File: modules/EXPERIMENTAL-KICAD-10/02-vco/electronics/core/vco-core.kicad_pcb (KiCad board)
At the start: 2 copper layers, 58 x 110 mm, 146 parts, among them J1 Conn_01x04, J2 Conn_02x05_Odd_Even, J3 Conn_02x05_Odd_Even, J4 Conn_01x02, J5 Conn_02x03_Odd_Even, J6 Conn_02x02_Counter_Clockwise, J8 Conn_01x07, Q1 BC847BS, Q2 MMBT3906, Q3 J111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

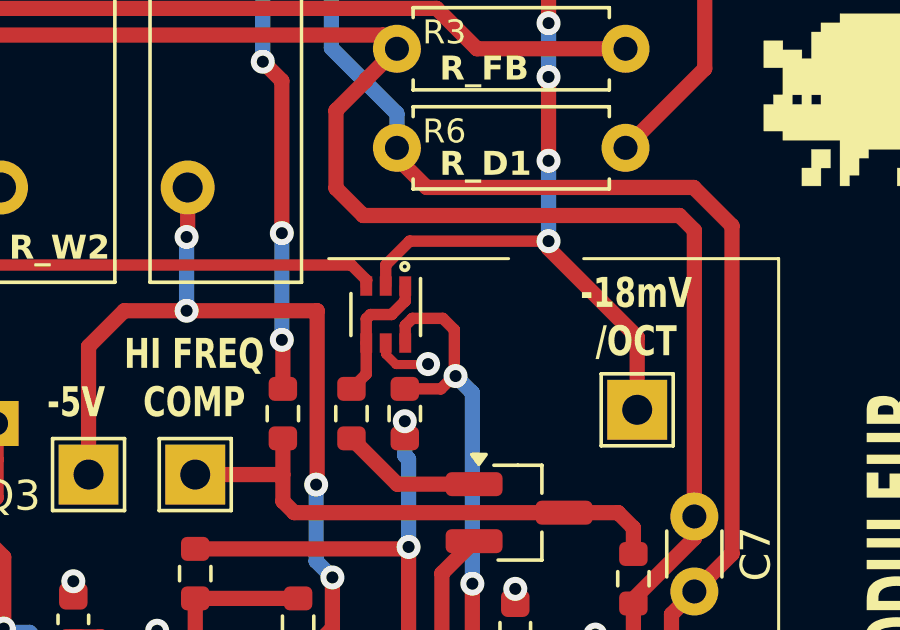
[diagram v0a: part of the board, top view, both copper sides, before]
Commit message: Updated experimental VCO Core
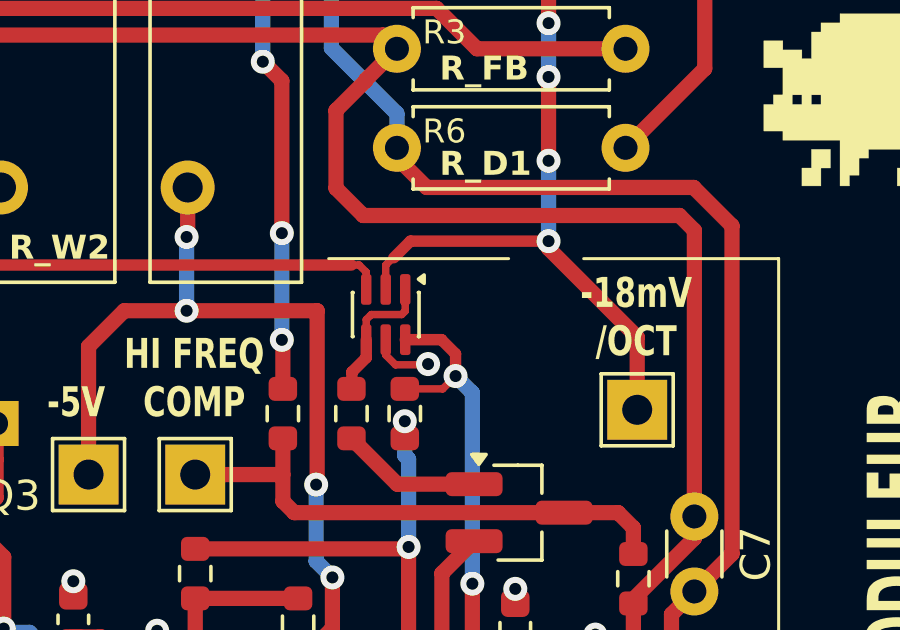
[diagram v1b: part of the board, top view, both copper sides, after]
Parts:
- Q1: footprint Shmoergh_Custom_Footprints:SOT-363_SC-70-6 -> Package_TO_SOT_SMD:SOT-363_SC-70-6
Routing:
- net /Raw oscillator/I_REF: track 32.2 -> 30.8 mm

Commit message: Revert "Updated experimental VCO Core"
This reverts commit 34f3e113d18d89390407e9554ee904153359fd81.
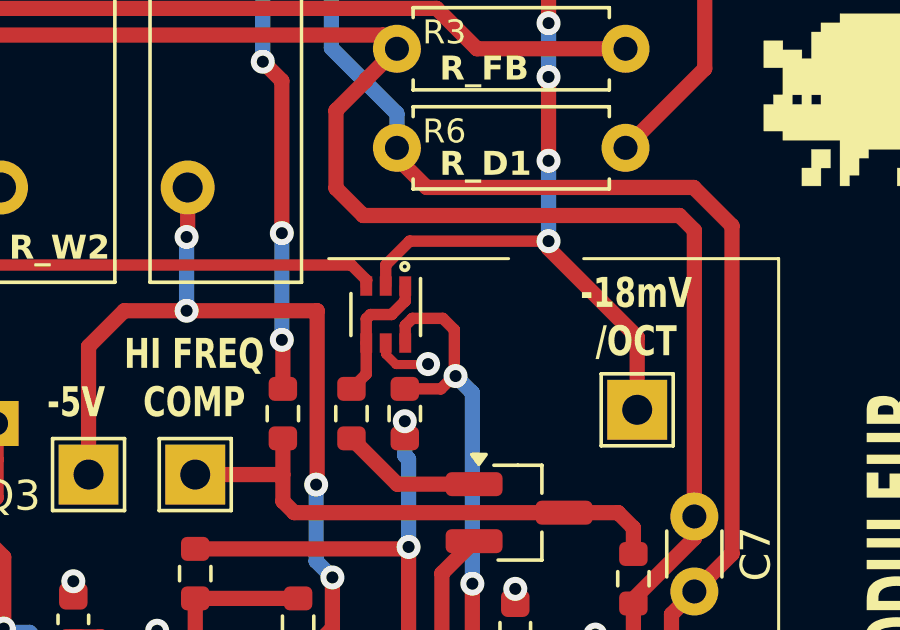
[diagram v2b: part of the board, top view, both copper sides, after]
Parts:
- Q1: footprint Package_TO_SOT_SMD:SOT-363_SC-70-6 -> Shmoergh_Custom_Footprints:SOT-363_SC-70-6
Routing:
- net /Raw oscillator/I_REF: track 30.8 -> 32.2 mm
